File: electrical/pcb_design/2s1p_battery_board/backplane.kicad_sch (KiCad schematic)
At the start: 37 parts, among them J1 TE_Connectivity_7-5530843-7, J10 TE_Connectivity_7-5530843-7, J11 TE_Connectivity_7-5530843-7, J12 TE_Connectivity_7-5530843-7, J13 TE_Connectivity_7-5530843-7, J14 TE_Connectivity_7-5530843-7, J15 TE_Connectivity_7-5530843-7, J16 TE_Connectivity_7-5530843-7, J2 TE_Connectivity_7-5530843-7, J3 TE_Connectivity_7-5530843-7, J4 TE_Connectivity_7-5530843-7, J5 TE_Connectivity_7-5530843-7, J6 TE_Connectivity_7-5530843-7, J7 TE_Connectivity_7-5530843-7, J8 TE_Connectivity_7-5530843-7, J9 TE_Connectivity_7-5530843-7, U3 TCAN330

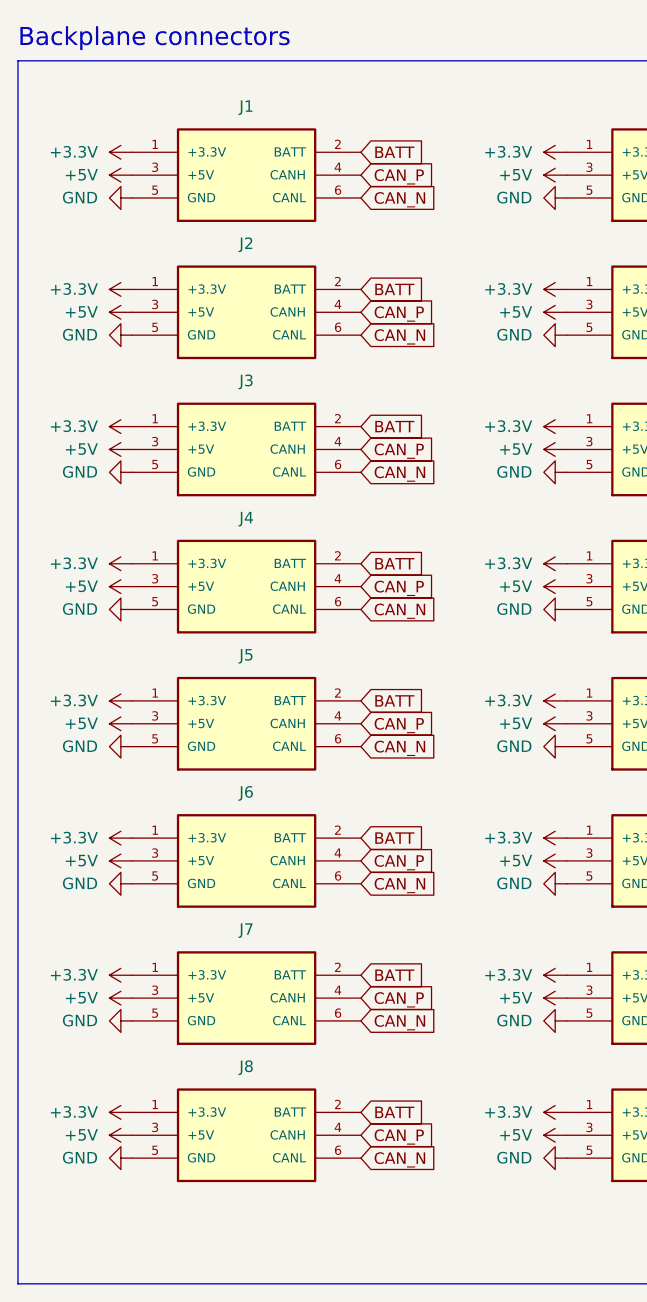
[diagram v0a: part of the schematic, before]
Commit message: Marked unconnected board edge connectors as 'NC'
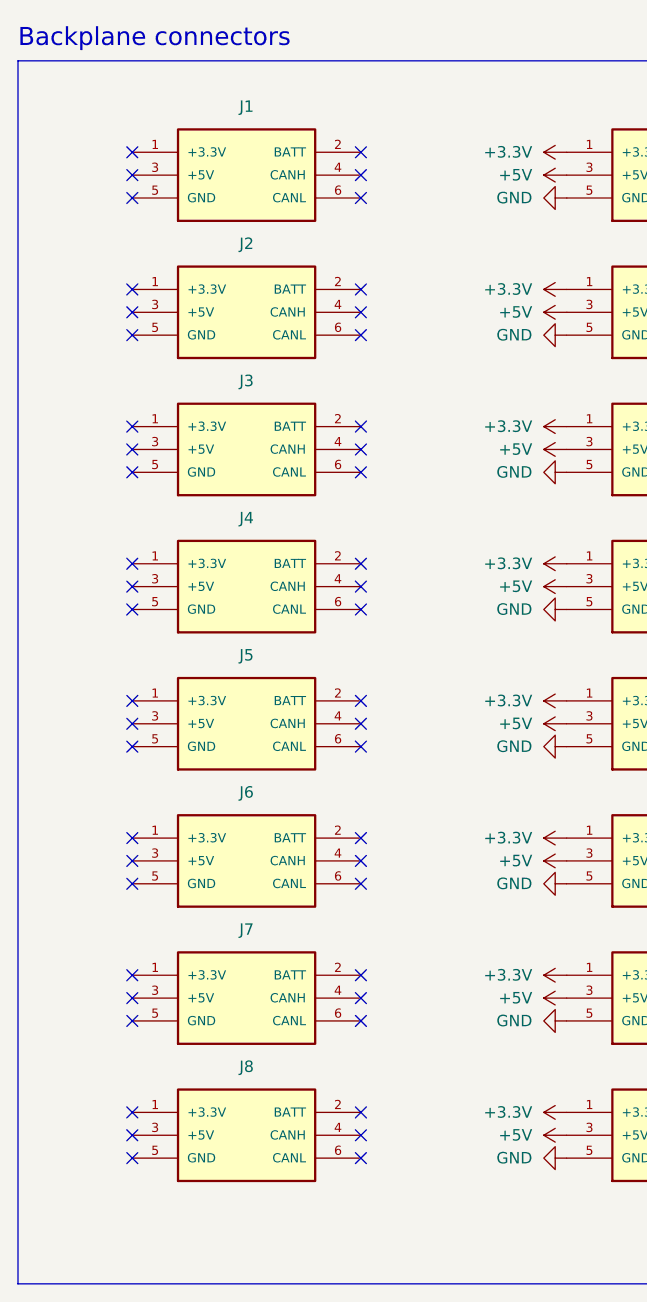
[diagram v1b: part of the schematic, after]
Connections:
- net +3.3V: no longer J1.1 (+3.3V), J2.1 (+3.3V), J3.1 (+3.3V), J4.1 (+3.3V), J5.1 (+3.3V), J6.1 (+3.3V), J7.1 (+3.3V), J8.1 (+3.3V)
- net +5V: no longer J1.3 (+5V), J2.3 (+5V), J3.3 (+5V), J4.3 (+5V), J5.3 (+5V), J6.3 (+5V), J7.3 (+5V), J8.3 (+5V)
- net BATT: no longer J1.2 (BATT), J2.2 (BATT), J3.2 (BATT), J4.2 (BATT), J5.2 (BATT), J6.2 (BATT), J7.2 (BATT), J8.2 (BATT)
- net CAN_N: no longer J1.6 (CANL), J2.6 (CANL), J3.6 (CANL), J4.6 (CANL), J5.6 (CANL), J6.6 (CANL), J7.6 (CANL), J8.6 (CANL)
- net CAN_P: no longer J1.4 (CANH), J2.4 (CANH), J3.4 (CANH), J4.4 (CANH), J5.4 (CANH), J6.4 (CANH), J7.4 (CANH), J8.4 (CANH)
- net GND: no longer J1.5 (GND), J2.5 (GND), J3.5 (GND), J4.5 (GND), J5.5 (GND), J6.5 (GND), J7.5 (GND), J8.5 (GND)
- no-connect marks 2 -> 50

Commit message: Checkpointing work on battery boards
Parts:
- removed C7, C8: 10u, Capacitor_SMD:C_0603_1608Metric, symbol Device:C
- removed J1, J2, J3, J4, J5, J6, J7, J8: TE_Connectivity_7-5530843-7, footprints:TE_Connectivity_7-5530843-7, symbol TVSC:Backplane_Connector_Consumer
- removed JP1, JP2, JP3, JP4: SolderJumper_2_Open, Jumper:SolderJumper-2_P1.3mm_Bridged_RoundedPad1.0x1.5mm, symbol Jumper:SolderJumper_2_Open
- removed R5, R6, R7, R8: 60, Resistor_SMD:R_0402_1005Metric, symbol Device:R
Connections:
- no-connect marks 50 -> 2
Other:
- moved on the sheet: C10, C9, J10, J11, J12, J13, J14, J15, J16, J9, JP5, JP6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

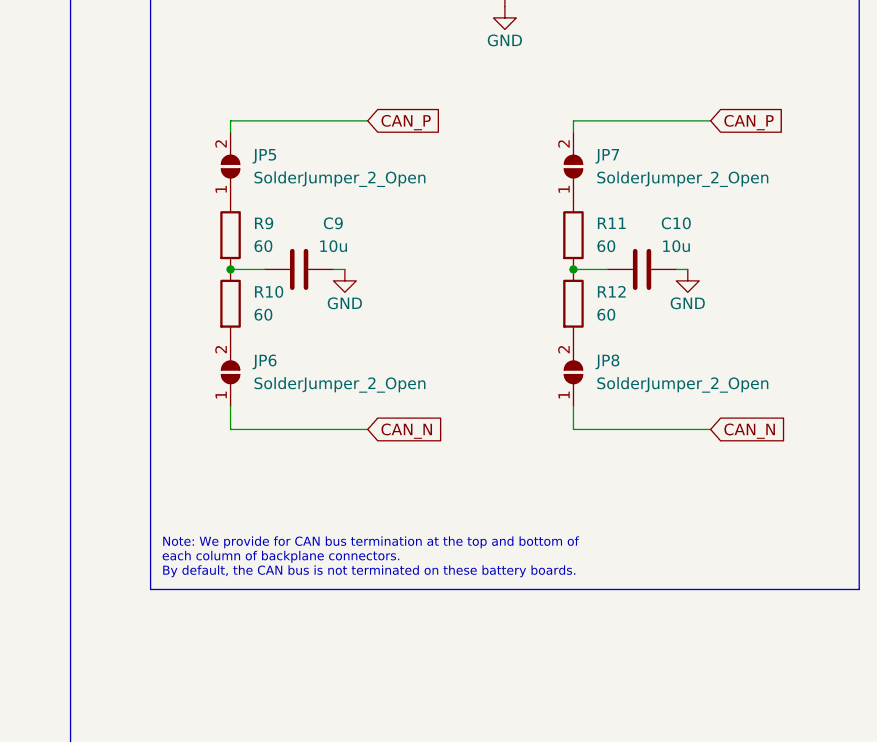
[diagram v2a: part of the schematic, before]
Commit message: Fixed CAN bus termination
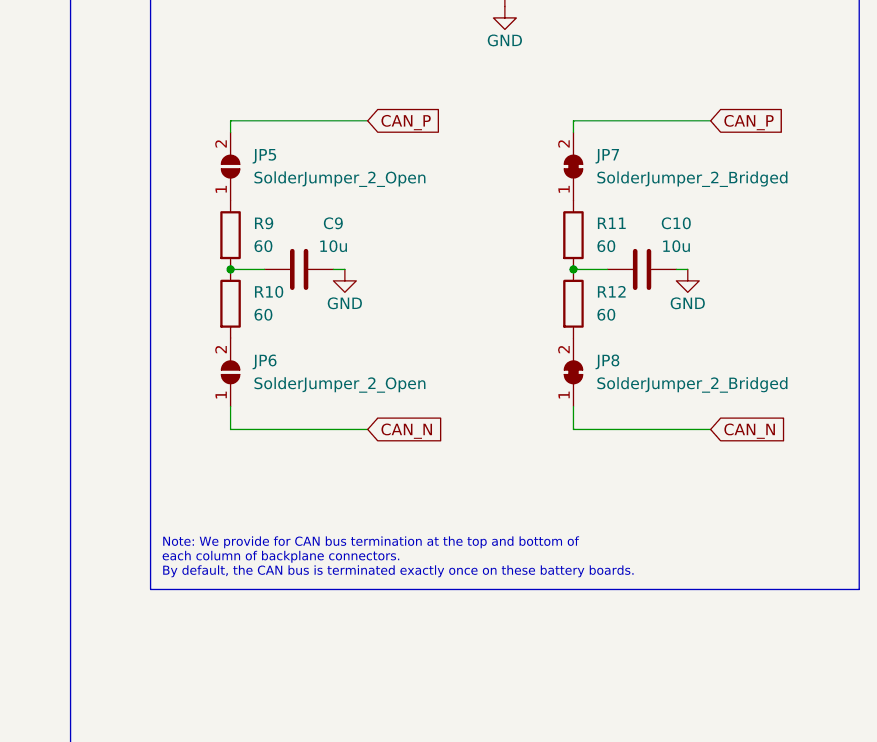
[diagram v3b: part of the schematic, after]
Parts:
- JP5, JP6: footprint Jumper:SolderJumper-2_P1.3mm_Bridged_RoundedPad1.0x1.5mm -> Jumper:SolderJumper-2_P1.3mm_Open_RoundedPad1.0x1.5mm
- JP7, JP8: value SolderJumper_2_Open -> SolderJumper_2_Bridged; symbol Jumper:SolderJumper_2_Open -> Jumper:SolderJumper_2_Bridged
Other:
- note added: "Note: We provide for CAN bus termination at the top and bottom of each column of backplane connectors. By default, the CAN bus is terminated exactly once on these battery boards."
- note removed: "Note: We provide for CAN bus termination at the top and bottom of each column of backplane connectors. By default, the CAN bus is not terminated on these battery boards."
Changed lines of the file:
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@@
     (effects (font (size 2 2)) (justify left bottom))
   )
-  (text "Note: We provide for CAN bus termination at the top and bottom of\neach column of backplane connectors.\nBy default, the CAN bus is not terminated on these battery boards."
+  (text "Note: We provide for CAN bus termination at the top and bottom of\neach column of backplane connectors.\nBy default, the CAN bus is terminated exactly once on these battery boards."
     (at 143.51 127 0)
     (effects (font (size 1 1)) (justify left bottom))
@@
       (effects (font (size 1.27 1.27)) (justify right))
     )
-    (property "Footprint" "Jumper:SolderJumper-2_P1.3mm_Bridged_RoundedPad1.0x1.5mm" (at 151.13 81.28 0)
+    (property "Footprint" "Jumper:SolderJumper-2_P1.3mm_Open_RoundedPad1.0x1.5mm" (at 151.13 81.28 0)
       (effects (font (size 1.27 1.27)) hide)
     )
@@
     )
   )
-  (symbol (lib_id "Jumper:SolderJumper_2_Open") (at 189.23 104.14 90) (unit 1)
+  (symbol (lib_id "Jumper:SolderJumper_2_Bridged") (at 189.23 104.14 90) (unit 1)
     (in_bom yes) (on_board yes) (dnp no) (fields_autoplaced)
     (property "Reference" "JP8" (at 191.77 102.87 90)
       (effects (font (size 1.27 1.27)) (justify right))
     )
-    (property "Value" "SolderJumper_2_Open" (at 191.77 105.41 90)
+    (property "Value" "SolderJumper_2_Bridged" (at 191.77 105.41 90)
       (effects (font (size 1.27 1.27)) (justify right))
     )
@@
     )
   )
-  (symbol (lib_id "Jumper:SolderJumper_2_Open") (at 189.23 81.28 90) (unit 1)
+  (symbol (lib_id "Jumper:SolderJumper_2_Bridged") (at 189.23 81.28 90) (unit 1)
     (in_bom yes) (on_board yes) (dnp no) (fields_autoplaced)
     (property "Reference" "JP7" (at 191.77 80.01 90)
       (effects (font (size 1.27 1.27)) (justify right))
     )
-    (property "Value" "SolderJumper_2_Open" (at 191.77 82.55 90)
+    (property "Value" "SolderJumper_2_Bridged" (at 191.77 82.55 90)
       (effects (font (size 1.27 1.27)) (justify right))
     )
@@
       (effects (font (size 1.27 1.27)) (justify right))
     )
-    (property "Footprint" "Jumper:SolderJumper-2_P1.3mm_Bridged_RoundedPad1.0x1.5mm" (at 151.13 104.14 0)
-      (effects (font (size 1.27 1.27)) hide)
-    )
+    (property "Footprint" "Jumper:SolderJumper-2_P1.3mm_Open_RoundedPad1.0x1.5mm" (at 151.13 104.14 0)
+      (effects (font (size 1.27 1.27)) hide)
+    )

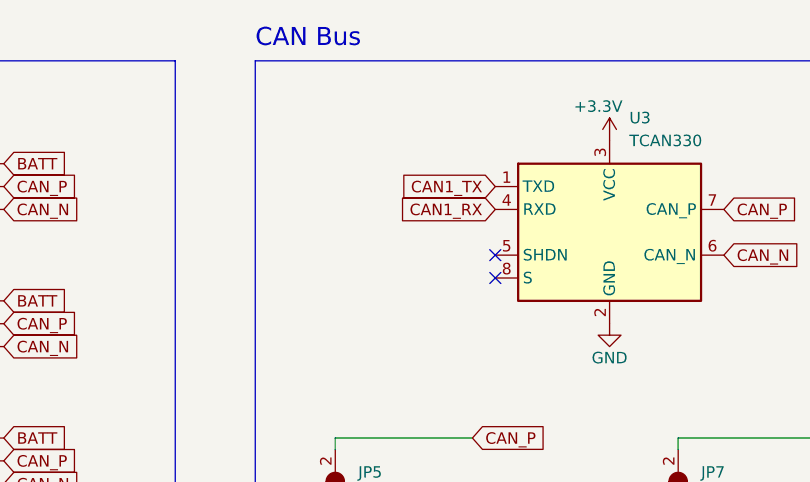
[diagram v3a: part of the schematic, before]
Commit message: Activate secondary backplane in the event that we decide to use it on another board. This will prevent a turn of this board in that event.
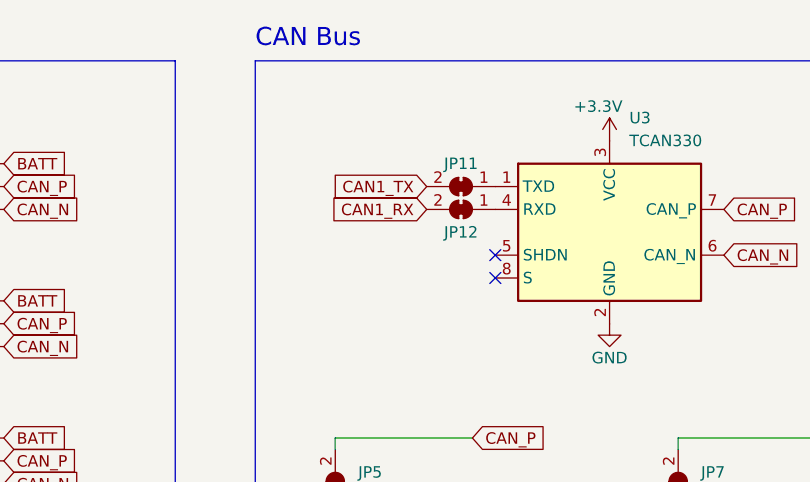
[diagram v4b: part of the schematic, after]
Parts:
- added JP11, JP12: SolderJumper_2_Bridged, Jumper:SolderJumper-2_P1.3mm_Bridged_RoundedPad1.0x1.5mm, symbol Jumper:SolderJumper_2_Bridged
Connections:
- net CAN1_RX: now also JP12.2 (B); no longer U3.4 (RXD)
- net CAN1_TX: now also JP11.2 (B); no longer U3.1 (TXD)
- new net: JP11.1 (A), U3.1 (TXD)
- new net: JP12.1 (A), U3.4 (RXD)
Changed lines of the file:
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@@
+    )
+  )
+  (global_label "CAN1_RX" (shape input) (at 161.29 50.8 180) (fields_autoplaced)
+    (effects (font (size 1.27 1.27)) (justify right))
+    (property "Intersheetrefs" "${INTERSHEET_REFS}" (at 149.9591 50.8 0)
+      (effects (font (size 1.27 1.27)) (justify right) hide)
     )
   )
@@
     )
   )
-  (global_label "CAN1_RX" (shape input) (at 168.91 50.8 180) (fields_autoplaced)
+  (global_label "CAN1_TX" (shape input) (at 161.29 48.26 180) (fields_autoplaced)
     (effects (font (size 1.27 1.27)) (justify right))
-    (property "Intersheetrefs" "${INTERSHEET_REFS}" (at 157.5791 50.8 0)
+    (property "Intersheetrefs" "${INTERSHEET_REFS}" (at 150.2615 48.26 0)
       (effects (font (size 1.27 1.27)) (justify right) hide)
     )
@@
     (property "Intersheetrefs" "${INTERSHEET_REFS}" (at 212.1724 110.49 0)
       (effects (font (size 1.27 1.27)) (justify left) hide)
-    )
-  )
-  (global_label "CAN1_TX" (shape input) (at 168.91 48.26 180) (fields_autoplaced)
-    (effects (font (size 1.27 1.27)) (justify right))
-    (property "Intersheetrefs" "${INTERSHEET_REFS}" (at 157.8815 48.26 0)
-      (effects (font (size 1.27 1.27)) (justify right) hide)
     )
   )
@@
     )
   )
+  (symbol (lib_id "Jumper:SolderJumper_2_Bridged") (at 165.1 48.26 180) (unit 1)
+    (in_bom yes) (on_board yes) (dnp no)
+    (property "Reference" "JP11" (at 165.1 45.72 0)
+      (effects (font (size 1.27 1.27)))
+    )
+    (property "Value" "SolderJumper_2_Bridged" (at 165.1 44.45 0)
+      (effects (font (size 1.27 1.27)) hide)
+    )
+    (property "Footprint" "Jumper:SolderJumper-2_P1.3mm_Bridged_RoundedPad1.0x1.5mm" (at 165.1 48.26 0)
+      (effects (font (size 1.27 1.27)) hide)
+    )
+    (property "Datasheet" "~" (at 165.1 48.26 0)
+      (effects (font (size 1.27 1.27)) hide)
+    )
+    (pin "1")
+    (pin "2")
+    (instances
+      (project "2s1p_battery_board"
+        (path "/33b6cfb5-4243-4b65-baae-021998c06cfa/14795c5f-6fe1-4dc3-a95c-48687b8f8872"
+          (reference "JP11") (unit 1)
+        )
+      )
+    )
+  )
   (symbol (lib_id "power:+5V") (at 88.9 109.22 90) (unit 1)
     (in_bom yes) (on_board yes) (dnp no) (fields_autoplaced)
@@
         )
       )
+    )
+  )
+  (symbol (lib_id "Jumper:SolderJumper_2_Bridged") (at 165.1 50.8 180) (unit 1)
+    (in_bom yes) (on_board yes) (dnp no)
+    (property "Reference" "JP12" (at 165.1 53.34 0)
+      (effects (font (size 1.27 1.27)))
+    )
+    (property "Value" "SolderJumper_2_Bridged" (at 165.1 46.99 0)
+      (effects (font (size 1.27 1.27)) hide)
+    )
+    (property "Footprint" "Jumper:SolderJumper-2_P1.3mm_Bridged_RoundedPad1.0x1.5mm" (at 165.1 50.8 0)
+      (effects (font (size 1.27 1.27)) hide)
+    )
+    (property "Datasheet" "~" (at 165.1 50.8 0)
+      (effects (font (size 1.27 1.27)) hide)
+    )
+    (pin "1")
+    (pin "2")
+    (instances
+      (project "2s1p_battery_board"
+        (path "/33b6cfb5-4243-4b65-baae-021998c06cfa/14795c5f-6fe1-4dc3-a95c-48687b8f8872"
+          (reference "JP12") (unit 1)
+        )
+      )

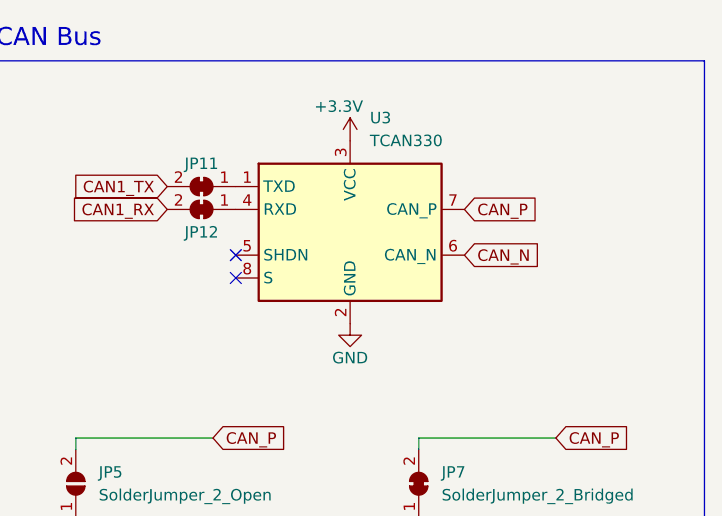
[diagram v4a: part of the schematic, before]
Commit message: Verified schematics and PCBs for all boards
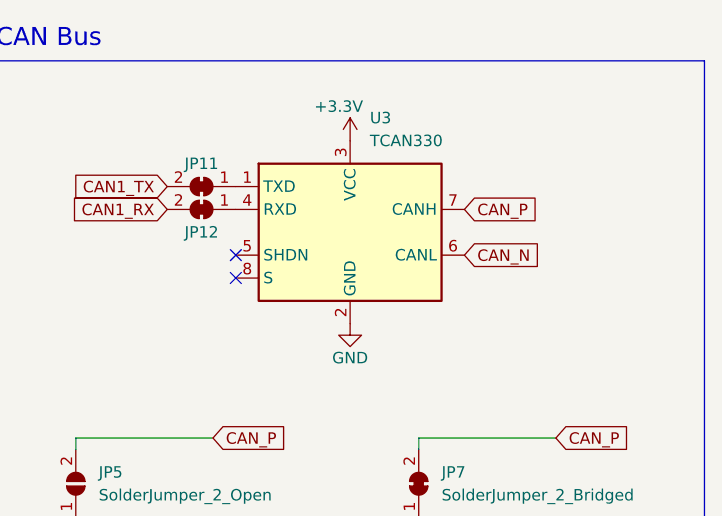
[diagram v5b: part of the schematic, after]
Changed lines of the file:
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@@
       (effects (font (size 1.27 1.27) italic) hide)
     )
-    (property "Datasheet" "https://www.ti.com/lit/ds/symlink/tcan330.pdf" (at 181.61 53.34 0)
+    (property "Datasheet" "http://www.ti.com/lit/ds/symlink/tcan337.pdf" (at 181.61 53.34 0)
       (effects (font (size 1.27 1.27)) hide)
     )
